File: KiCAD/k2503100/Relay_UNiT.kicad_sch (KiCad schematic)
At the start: 0 parts

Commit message: 途中 Relay Unit
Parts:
- added J10, J9: Analog, Connector_PinSocket_2.54mm:PinSocket_1x08_P2.54mm_Vertical, symbol Connector_Generic:Conn_01x08
- added J11: Digital, Connector_PinSocket_2.54mm:PinSocket_2x18_P2.54mm_Vertical, symbol Connector_Generic:Conn_02x18_Odd_Even
- added J12: PWM, Connector_PinSocket_2.54mm:PinSocket_1x10_P2.54mm_Vertical, symbol Connector_Generic:Conn_01x10
- added J13: PWM, Connector_PinSocket_2.54mm:PinSocket_1x08_P2.54mm_Vertical, symbol Connector_Generic:Conn_01x08
- added J14: Communication, Connector_PinSocket_2.54mm:PinSocket_1x08_P2.54mm_Vertical, symbol Connector_Generic:Conn_01x08
- added J22: RELAY-1, symbol Connector_Generic:Conn_02x10_Odd_Even
- added J23: RELAY-2, symbol Connector_Generic:Conn_02x10_Odd_Even
- added J24: RELAY-3, symbol Connector_Generic:Conn_02x10_Odd_Even
- added J25: RELAY-4, symbol Connector_Generic:Conn_02x10_Odd_Even
- added J8: Power, Connector_PinSocket_2.54mm:PinSocket_1x08_P2.54mm_Vertical, symbol Connector_Generic:Conn_01x08
- added RV1: DELAY1, symbol Device:R_Potentiometer_US
- added RV2: DELAY2, symbol Device:R_Potentiometer_US
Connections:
- new net *10: J12.8 (Pin_8)
- new net *11: J12.7 (Pin_7)
- new net *12: J12.6 (Pin_6)
- new net *13: J12.5 (Pin_5)
- new net *2: J13.6 (Pin_6)
- new net *3: J13.5 (Pin_5)
- new net *4: J13.4 (Pin_4)
- new net *44: J11.11 (Pin_11)
- new net *45: J11.12 (Pin_12)
- new net *46: J11.9 (Pin_9)
- new net *5: J13.3 (Pin_3)
- new net *52: J11.3 (Pin_3)
- new net *6: J13.2 (Pin_2)
- new net *7: J13.1 (Pin_1)
- new net *8: J12.10 (Pin_10)
- new net *9: J12.9 (Pin_9)
- new net +3V3: J8.4 (Pin_4)
- new net +5V: J11.35 (Pin_35), J11.36 (Pin_36), J22.1 (Pin_1), J22.2 (Pin_2), J23.1 (Pin_1), J23.2 (Pin_2), J24.1 (Pin_1), J24.2 (Pin_2), J25.1 (Pin_1), J25.2 (Pin_2), J8.5 (Pin_5), RV1.1, RV2.1
- new net 22: J11.33 (Pin_33)
- new net 23: J11.34 (Pin_34)
- new net 24: J11.31 (Pin_31)
- new net 25: J11.32 (Pin_32)
- new net 26: J11.29 (Pin_29)
- new net 27: J11.30 (Pin_30)
- new net 28: J11.27 (Pin_27)
- new net 29: J11.28 (Pin_28)
- new net 30: J11.25 (Pin_25)
- new net 31: J11.26 (Pin_26)
- new net 32: J11.23 (Pin_23)
- new net 33: J11.24 (Pin_24)
- new net 34: J11.21 (Pin_21)
- new net 35: J11.22 (Pin_22)
- new net 36: J11.19 (Pin_19)
- new net 37: J11.20 (Pin_20)
- new net 38: J11.17 (Pin_17)
- new net 39: J11.18 (Pin_18)
- new net 40: J11.15 (Pin_15)
- new net 41: J11.16 (Pin_16)
- new net 42: J11.13 (Pin_13)
- new net 43: J11.14 (Pin_14)
- new net 47: J11.10 (Pin_10)
- new net 48: J11.7 (Pin_7)
- new net 49: J11.8 (Pin_8)
- new net 50: J11.5 (Pin_5)
- new net 51: J11.6 (Pin_6)
- new net 53: J11.4 (Pin_4)
- new net A0: J9.1 (Pin_1)
- new net A1: J9.2 (Pin_2)
- new net A10: J10.3 (Pin_3)
- new net A11: J10.4 (Pin_4)
- new net A12: J10.5 (Pin_5)
- new net A13: J10.6 (Pin_6)
- new net A14: J10.7 (Pin_7), RV1.2
- new net A15: J10.8 (Pin_8), RV2.2
- new net A2: J9.3 (Pin_3)
- new net A3: J9.4 (Pin_4)
- new net A4: J9.5 (Pin_5)
- new net A5: J9.6 (Pin_6)
- new net A6: J9.7 (Pin_7)
- new net A7: J9.8 (Pin_8)
- new net A8: J10.1 (Pin_1)
- new net A9: J10.2 (Pin_2)
- new net AREF: J12.3 (Pin_3)
- new net GND: J11.1 (Pin_1), J11.2 (Pin_2), J12.4 (Pin_4), J22.19 (Pin_19), J22.20 (Pin_20), J23.19 (Pin_19), J23.20 (Pin_20), J24.19 (Pin_19), J24.20 (Pin_20), J25.19 (Pin_19), J25.20 (Pin_20), J8.6 (Pin_6), J8.7 (Pin_7), RV1.3, RV2.3
- new net IOREF: J8.2 (Pin_2)
- new net RX0/0: J13.8 (Pin_8)
- new net RX1/19: J14.6 (Pin_6)
- new net RX2/17: J14.4 (Pin_4)
- new net RX3/15: J14.2 (Pin_2)
- new net SCL: J12.1 (Pin_1), J14.8 (Pin_8)
- new net SDA: J12.2 (Pin_2), J14.7 (Pin_7)
- new net TX0/1: J13.7 (Pin_7)
- new net TX1/18: J14.5 (Pin_5)
- new net TX2/16: J14.3 (Pin_3)
- new net TX3/14: J14.1 (Pin_1)
- new net VCC: J8.8 (Pin_8)
- new net ~{RESET}: J8.3 (Pin_3)
- no-connect marks 0 -> 3
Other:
- company: (none) -> HOLLY&Co.,Ltd.
- title: (none) -> Relay Unit

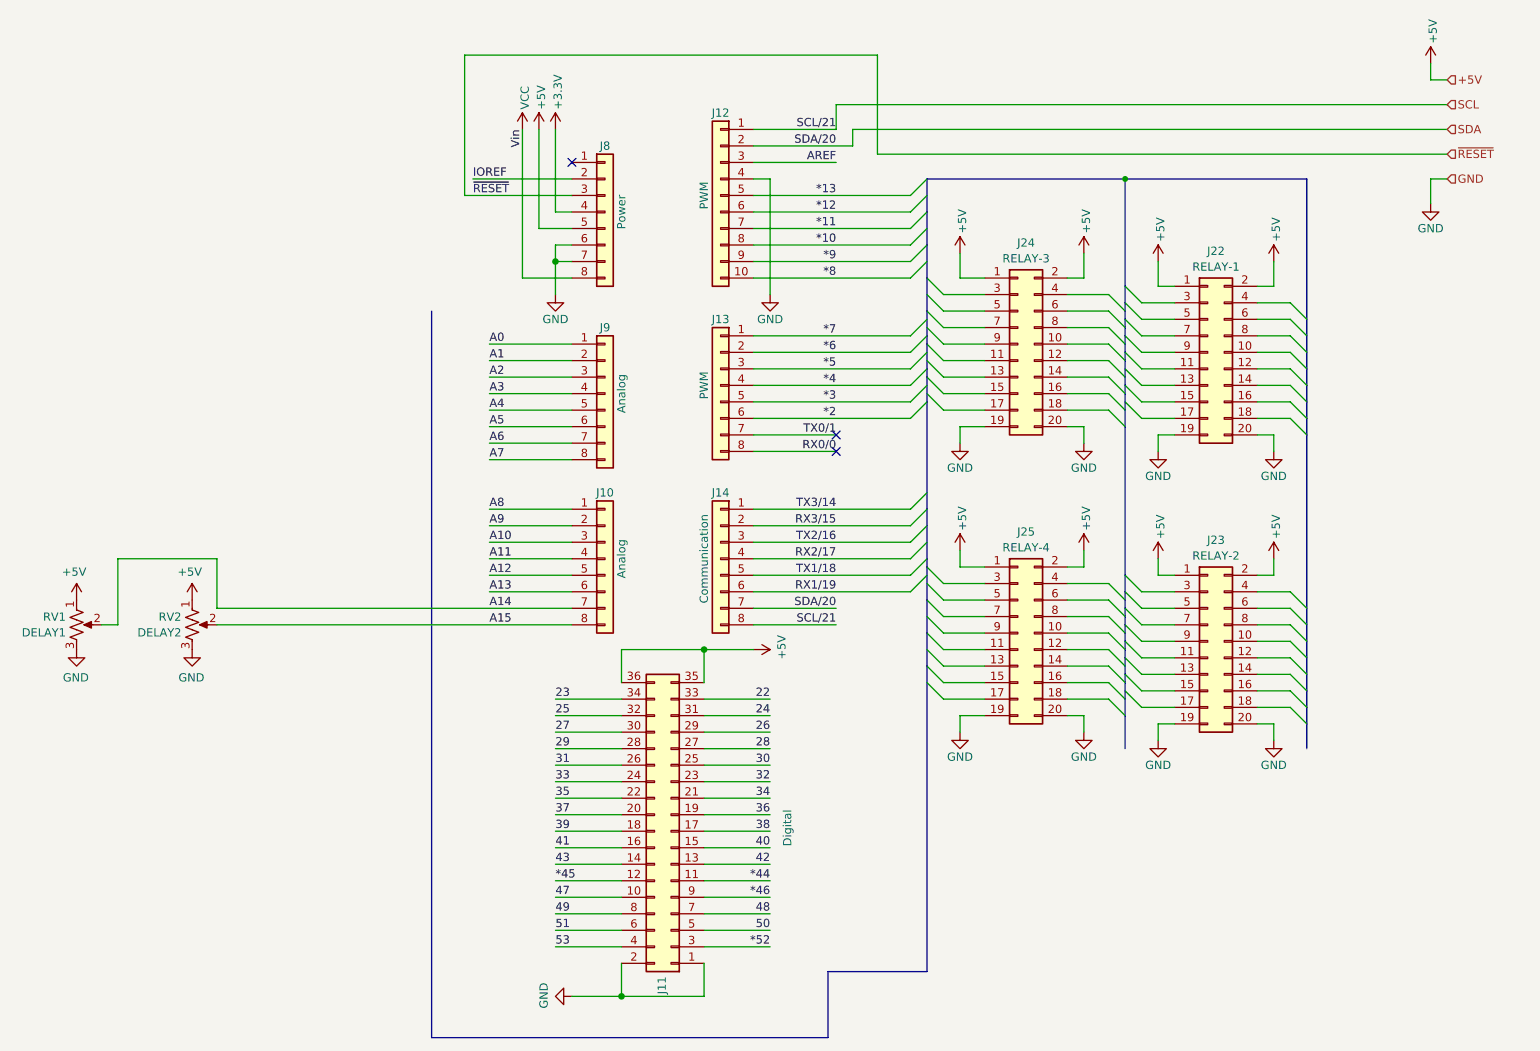
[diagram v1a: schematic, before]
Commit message: Relay_UNiTの端子名入れ途中
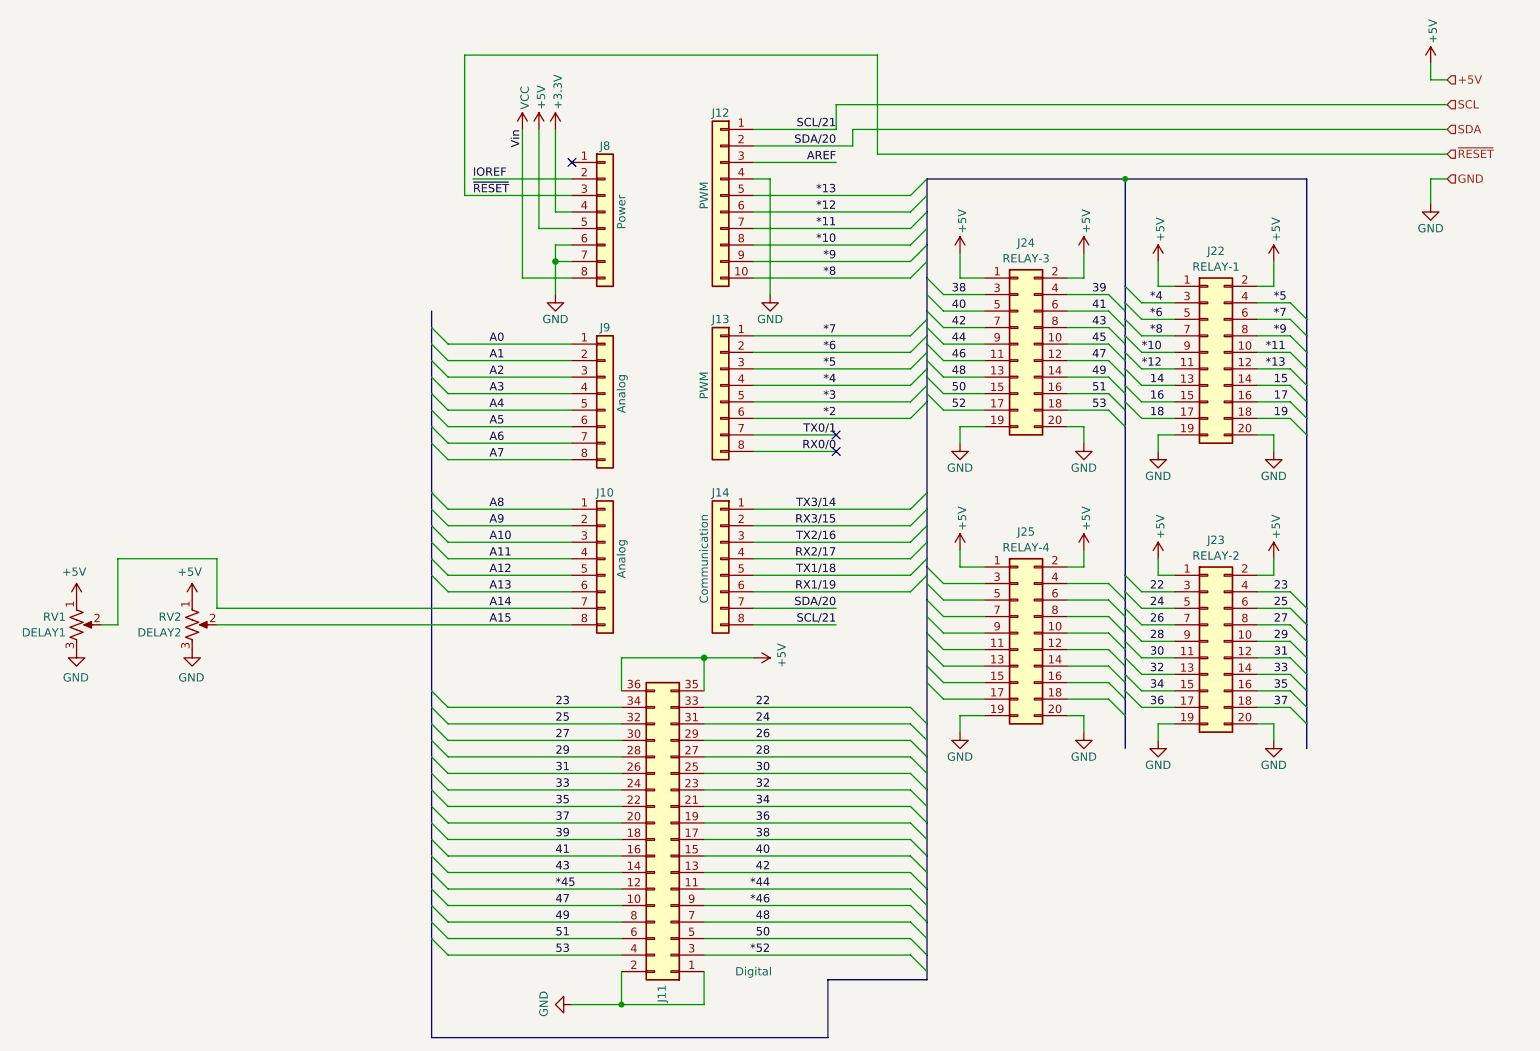
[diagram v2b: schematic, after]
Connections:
- net *10: now also J22.9 (Pin_9)
- net *11: now also J22.10 (Pin_10)
- net *12: now also J22.11 (Pin_11)
- net *13: now also J22.12 (Pin_12)
- net *4: now also J22.3 (Pin_3)
- net *5: now also J22.4 (Pin_4)
- net *6: now also J22.5 (Pin_5)
- net *7: now also J22.6 (Pin_6)
- net *8: now also J22.7 (Pin_7)
- net *9: now also J22.8 (Pin_8)
- net 22: now also J23.3 (Pin_3)
- net 23: now also J23.4 (Pin_4)
- net 24: now also J23.5 (Pin_5)
- net 25: now also J23.6 (Pin_6)
- net 26: now also J23.7 (Pin_7)
- net 27: now also J23.8 (Pin_8)
- net 28: now also J23.9 (Pin_9)
- net 29: now also J23.10 (Pin_10)
- net 30: now also J23.11 (Pin_11)
- net 31: now also J23.12 (Pin_12)
- net 32: now also J23.13 (Pin_13)
- net 33: now also J23.14 (Pin_14)
- net 34: now also J23.15 (Pin_15)
- net 35: now also J23.16 (Pin_16)
- net 36: now also J23.17 (Pin_17)
- net 37: now also J23.18 (Pin_18)
- net 38: now also J24.3 (Pin_3)
- net 39: now also J24.4 (Pin_4)
- net 40: now also J24.5 (Pin_5)
- net 41: now also J24.6 (Pin_6)
- net 42: now also J24.7 (Pin_7)
- net 43: now also J24.8 (Pin_8)
- net 47: now also J24.12 (Pin_12)
- net 48: now also J24.13 (Pin_13)
- net 49: now also J24.14 (Pin_14)
- net 50: now also J24.15 (Pin_15)
- net 51: now also J24.16 (Pin_16)
- net 53: now also J24.18 (Pin_18)
- net 14: now reaches J22.13 (Pin_13)
- net 15: now reaches J22.14 (Pin_14)
- net 16: now reaches J22.15 (Pin_15)
- net 17: now reaches J22.16 (Pin_16)
- net 18: now reaches J22.17 (Pin_17)
- net 19: now reaches J22.18 (Pin_18)
- net 45: now reaches J24.10 (Pin_10)
- net 46: now reaches J24.11 (Pin_11)
- net 52: now reaches J24.17 (Pin_17)
- net 44: now reaches J24.9 (Pin_9)
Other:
- moved on the sheet: J11

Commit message: KiCAD 8
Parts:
- renumbered J9 to J10, J10 to J11, J11 to J8, J8 to J9
